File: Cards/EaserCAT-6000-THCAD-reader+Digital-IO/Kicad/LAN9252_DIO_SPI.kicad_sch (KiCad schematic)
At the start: 26 parts, among them CN3 0.1uF, U5 LAN9252_PT, Y1 25MHz

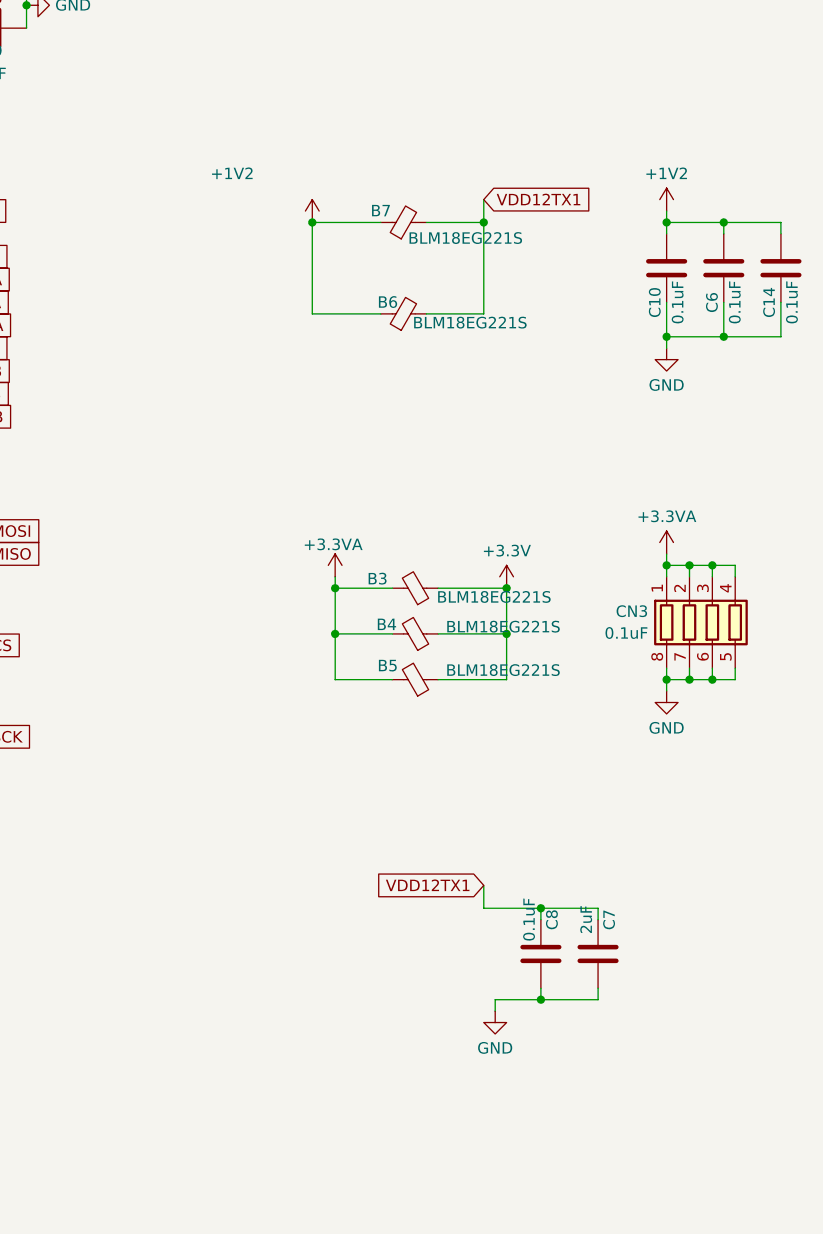
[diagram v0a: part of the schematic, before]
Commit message: Modified, switch marker postions for C28 and R17
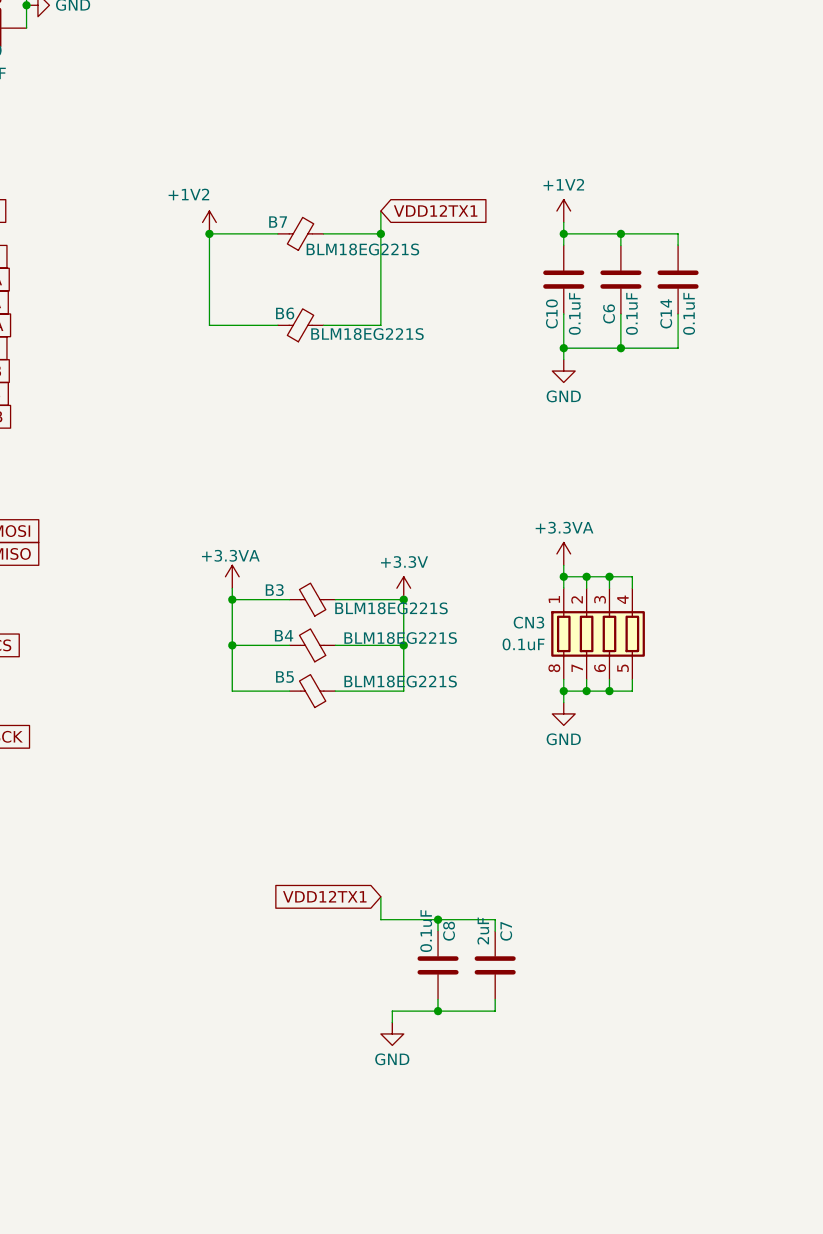
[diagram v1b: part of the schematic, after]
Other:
- moved on the sheet: B3, B4, B5, B6, B7, C10, C14, C6, C7, C8, CN3
